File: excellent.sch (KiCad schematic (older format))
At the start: 2 parts

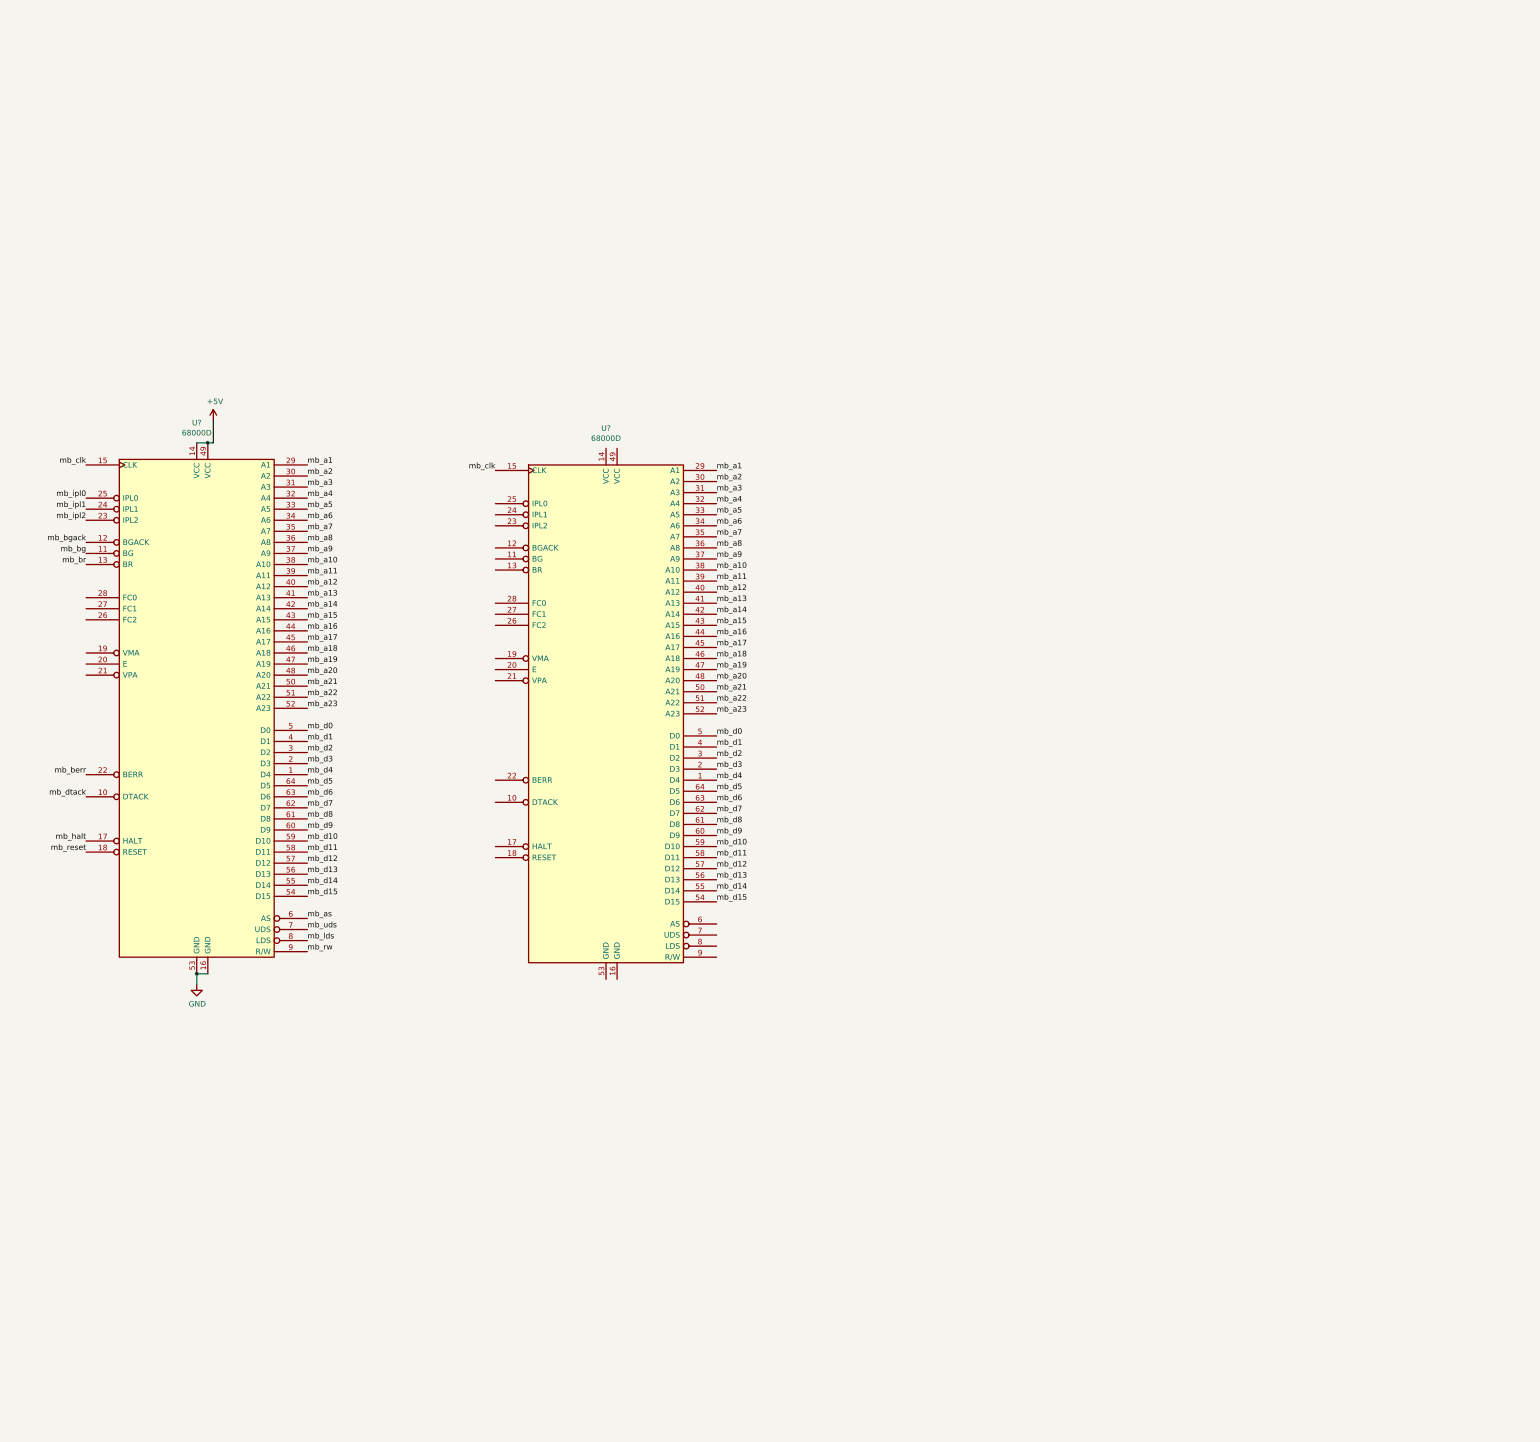
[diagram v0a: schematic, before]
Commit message: add 68040
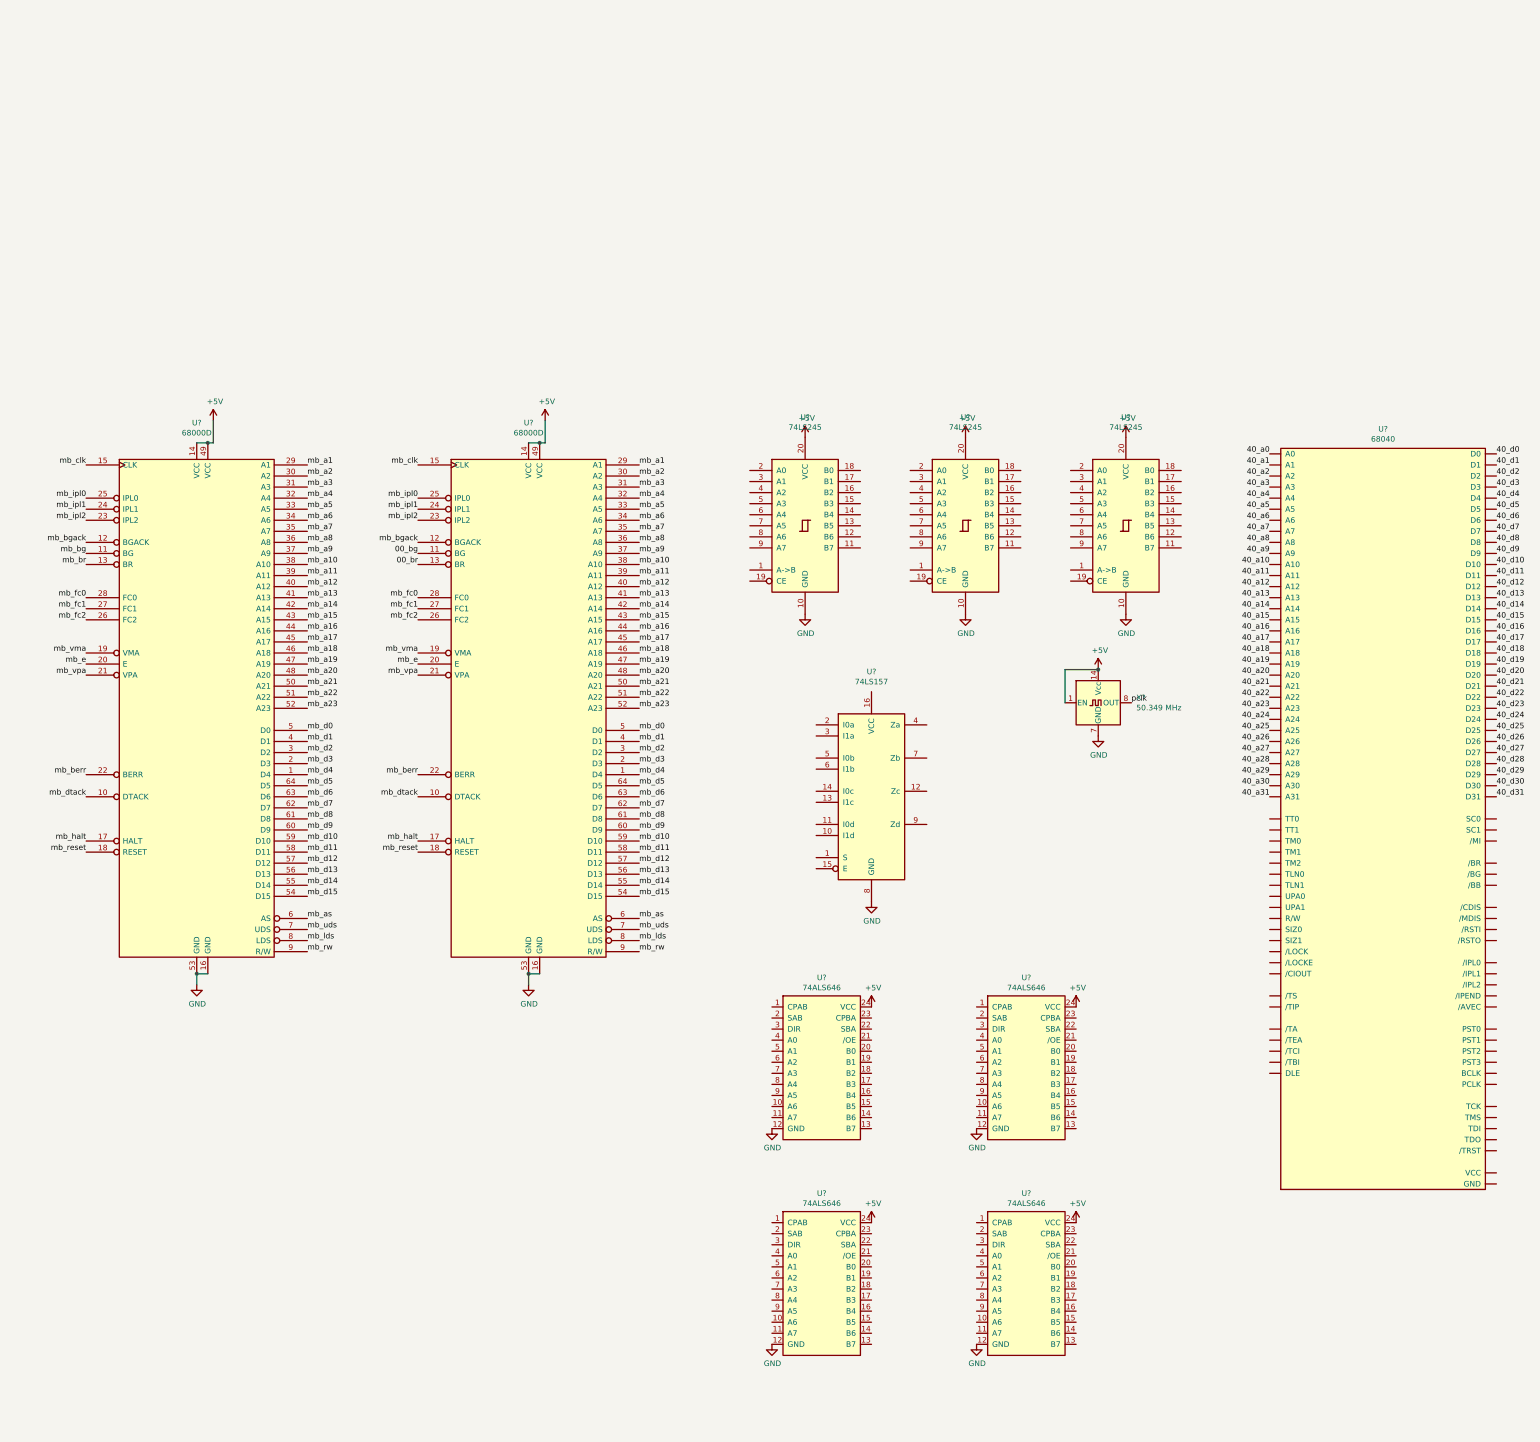
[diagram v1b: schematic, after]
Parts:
- removed U?: 68000D, symbol CPU_NXP_68000:68000D
- added U?: 68000D, symbol CPU_NXP_68000:68000D
- added U?: 68040, symbol excellent:68040
- added U? (x3): 74LS245, symbol 74xx:74LS245
- added U?: 74LS157, symbol 74xx:74LS157
- added U? (x4): 74ALS646, symbol excellent:74ALS646
- added X?: 50.349 MHz, Oscillator:Oscillator_DIP-14, symbol Oscillator:CXO_DIP14
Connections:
- net +5V: now also U?.14 (VCC), U?.20 (VCC), U?.20 (VCC), U?.20 (VCC), U?.24 (VCC), U?.24 (VCC), U?.24 (VCC), U?.24 (VCC), U?.49 (VCC), X?.1 (EN), X?.14 (Vcc)
- net GND: now also U?.10 (GND), U?.10 (GND), U?.10 (GND), U?.12 (GND), U?.12 (GND), U?.12 (GND), U?.12 (GND), U?.16 (GND), U?.53 (GND), U?.8 (GND), X?.7 (GND)
- net mb_a1: now also U?.29 (A1)
- net mb_a10: now also U?.38 (A10)
- net mb_a11: now also U?.39 (A11)
- net mb_a12: now also U?.40 (A12)
- net mb_a13: now also U?.41 (A13)
- net mb_a14: now also U?.42 (A14)
- net mb_a15: now also U?.43 (A15)
- net mb_a16: now also U?.44 (A16)
- net mb_a17: now also U?.45 (A17)
- net mb_a18: now also U?.46 (A18)
- net mb_a19: now also U?.47 (A19)
- net mb_a2: now also U?.30 (A2)
- net mb_a20: now also U?.48 (A20)
- net mb_a21: now also U?.50 (A21)
- net mb_a22: now also U?.51 (A22)
- net mb_a23: now also U?.52 (A23)
- net mb_a3: now also U?.31 (A3)
- net mb_a4: now also U?.32 (A4)
- net mb_a5: now also U?.33 (A5)
- net mb_a6: now also U?.34 (A6)
- net mb_a7: now also U?.35 (A7)
- net mb_a8: now also U?.36 (A8)
- net mb_a9: now also U?.37 (A9)
- net mb_as: now also U?.6 (AS)
- net mb_berr: now also U?.22 (BERR)
- net mb_bgack: now also U?.12 (BGACK)
- net mb_clk: now also U?.15 (CLK)
- net mb_d0: now also U?.5 (D0)
- net mb_d1: now also U?.4 (D1)
- net mb_d10: now also U?.59 (D10)
- net mb_d11: now also U?.58 (D11)
- net mb_d12: now also U?.57 (D12)
- net mb_d13: now also U?.56 (D13)
- net mb_d14: now also U?.55 (D14)
- net mb_d15: now also U?.54 (D15)
- net mb_d2: now also U?.3 (D2)
- net mb_d3: now also U?.2 (D3)
- net mb_d4: now also U?.1 (D4)
- net mb_d5: now also U?.64 (D5)
- net mb_d6: now also U?.63 (D6)
- net mb_d7: now also U?.62 (D7)
- net mb_d8: now also U?.61 (D8)
- net mb_d9: now also U?.60 (D9)
- net mb_dtack: now also U?.10 (DTACK)
- net mb_halt: now also U?.17 (HALT)
- net mb_ipl0: now also U?.25 (IPL0)
- net mb_ipl1: now also U?.24 (IPL1)
- net mb_ipl2: now also U?.23 (IPL2)
- net mb_lds: now also U?.8 (LDS)
- net mb_reset: now also U?.18 (RESET)
- net mb_rw: now also U?.9 (R/W)
- net mb_uds: now also U?.7 (UDS)
- net mb_vma: now reaches U?.19 (VMA)
- net mb_vma: now also U?.19 (VMA)
- net mb_e: now reaches U?.20 (E)
- net mb_e: now also U?.20 (E)
- net mb_vpa: now reaches U?.21 (VPA)
- net mb_vpa: now also U?.21 (VPA)
- net mb_fc2: now reaches U?.26 (FC2)
- net mb_fc2: now also U?.26 (FC2)
- net mb_fc1: now reaches U?.27 (FC1)
- net mb_fc1: now also U?.27 (FC1)
- net mb_fc0: now reaches U?.28 (FC0)
- net mb_fc0: now also U?.28 (FC0)
- new net 00_bg: U?.11 (BG)
- new net 00_br: U?.13 (BR)
- new net 40_a0: U?.~ (VCC)
- new net 40_a1: U?.~ (VCC)
- new net 40_a10: U?.~ (VCC)
- new net 40_a11: U?.~ (VCC)
- new net 40_a12: U?.~ (VCC)
- new net 40_a13: U?.~ (VCC)
- new net 40_a14: U?.~ (VCC)
- new net 40_a15: U?.~ (VCC)
- new net 40_a16: U?.~ (VCC)
- new net 40_a17: U?.~ (VCC)
- new net 40_a18: U?.~ (VCC)
- new net 40_a19: U?.~ (VCC)
- new net 40_a2: U?.~ (VCC)
- new net 40_a20: U?.~ (VCC)
- new net 40_a21: U?.~ (VCC)
- new net 40_a22: U?.~ (VCC)
- new net 40_a23: U?.~ (VCC)
- new net 40_a24: U?.~ (VCC)
- new net 40_a25: U?.~ (VCC)
- new net 40_a26: U?.~ (VCC)
- new net 40_a27: U?.~ (VCC)
- new net 40_a28: U?.~ (VCC)
- new net 40_a29: U?.~ (VCC)
- new net 40_a3: U?.~ (VCC)
- new net 40_a30: U?.~ (VCC)
- new net 40_a31: U?.~ (VCC)
- new net 40_a4: U?.~ (VCC)
- new net 40_a5: U?.~ (VCC)
- new net 40_a6: U?.~ (VCC)
- new net 40_a7: U?.~ (VCC)
- new net 40_a8: U?.~ (VCC)
- new net 40_a9: U?.~ (VCC)
- new net 40_d0: U?.~ (VCC)
- new net 40_d1: U?.~ (VCC)
- new net 40_d10: U?.~ (VCC)
- new net 40_d11: U?.~ (VCC)
- new net 40_d12: U?.~ (VCC)
- new net 40_d13: U?.~ (VCC)
- new net 40_d14: U?.~ (VCC)
- new net 40_d15: U?.~ (VCC)
- new net 40_d16: U?.~ (VCC)
- new net 40_d17: U?.~ (VCC)
- new net 40_d18: U?.~ (VCC)
- new net 40_d19: U?.~ (VCC)
- new net 40_d2: U?.~ (VCC)
- new net 40_d20: U?.~ (VCC)
- new net 40_d21: U?.~ (VCC)
- new net 40_d22: U?.~ (VCC)
- new net 40_d23: U?.~ (VCC)
- new net 40_d24: U?.~ (VCC)
- new net 40_d25: U?.~ (VCC)
- new net 40_d26: U?.~ (VCC)
- new net 40_d27: U?.~ (VCC)
- new net 40_d28: U?.~ (VCC)
- new net 40_d29: U?.~ (VCC)
- new net 40_d3: U?.~ (VCC)
- new net 40_d30: U?.~ (VCC)
- new net 40_d31: U?.~ (VCC)
- new net 40_d4: U?.~ (VCC)
- new net 40_d5: U?.~ (VCC)
- new net 40_d6: U?.~ (VCC)
- new net 40_d7: U?.~ (VCC)
- new net 40_d8: U?.~ (VCC)
- new net 40_d9: U?.~ (VCC)
- new net pclk: X?.8 (OUT)

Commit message: wire up 646's
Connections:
- net 40_d0: now also U?.13 (B7)
- net 40_d1: now also U?.14 (B6)
- net 40_d10: now also U?.15 (B5)
- net 40_d11: now also U?.16 (B4)
- net 40_d12: now also U?.17 (B3)
- net 40_d13: now also U?.18 (B2)
- net 40_d14: now also U?.19 (B1)
- net 40_d15: now also U?.20 (B0)
- net 40_d16: now also U?.13 (B7)
- net 40_d17: now also U?.14 (B6)
- net 40_d18: now also U?.15 (B5)
- net 40_d19: now also U?.16 (B4)
- net 40_d2: now also U?.15 (B5)
- net 40_d20: now also U?.17 (B3)
- net 40_d21: now also U?.18 (B2)
- net 40_d22: now also U?.19 (B1)
- net 40_d23: now also U?.20 (B0)
- net 40_d24: now also U?.13 (B7)
- net 40_d25: now also U?.14 (B6)
- net 40_d26: now also U?.15 (B5)
- net 40_d27: now also U?.16 (B4)
- net 40_d28: now also U?.17 (B3)
- net 40_d29: now also U?.18 (B2)
- net 40_d3: now also U?.16 (B4)
- net 40_d30: now also U?.19 (B1)
- net 40_d31: now also U?.20 (B0)
- net 40_d4: now also U?.17 (B3)
- net 40_d5: now also U?.18 (B2)
- net 40_d6: now also U?.19 (B1)
- net 40_d7: now also U?.20 (B0)
- net 40_d9: now also U?.14 (B6)
- net at U?.1 (CPAB): now also U?.1 (CPAB), U?.23 (CPBA), U?.23 (CPBA) (x2)
- net 00_d1: now reaches U?.10 (A6)
- net 00_d1: now also U?.10 (A6)
- net 00_d0: now reaches U?.11 (A7)
- net 00_d0: now also U?.11 (A7)
- net at U?.2 (SAB): now also U?.2 (SAB) (x2)
- net at U?.21 (/OE): now also U?.21 (/OE) (x2)
- net at U?.22 (SBA): now also U?.22 (SBA) (x2)
- net at U?.3 (DIR): now also U?.3 (DIR) (x2)
- net 00_d7: now reaches U?.4 (A0)
- net 00_d7: now also U?.4 (A0)
- net 00_d6: now reaches U?.5 (A1)
- net 00_d6: now also U?.5 (A1)
- net 00_d5: now reaches U?.6 (A2)
- net 00_d5: now also U?.6 (A2)
- net 00_d4: now reaches U?.7 (A3)
- net 00_d4: now also U?.7 (A3)
- net 00_d3: now reaches U?.8 (A4)
- net 00_d3: now also U?.8 (A4)
- net 00_d2: now reaches U?.9 (A5)
- net 00_d2: now also U?.9 (A5)
- net 00_d10: now reaches U?.10 (A6)
- net 00_d10: now also U?.10 (A6)
- net 00_d9: now reaches U?.11 (A7)
- net 00_d9: now also U?.11 (A7)
- net 00_d16: now reaches U?.4 (A0)
- net 00_d16: now also U?.4 (A0)
- net 00_d15: now reaches U?.5 (A1)
- net 00_d15: now also U?.5 (A1)
- net 00_d14: now reaches U?.6 (A2)
- net 00_d14: now also U?.6 (A2)
- net 00_d13: now reaches U?.7 (A3)
- net 00_d13: now also U?.7 (A3)
- net 00_d12: now reaches U?.8 (A4)
- net 00_d12: now also U?.8 (A4)
- net 00_d11: now reaches U?.9 (A5)
- net 00_d11: now also U?.9 (A5)
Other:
- moved on the sheet: U?, X?
